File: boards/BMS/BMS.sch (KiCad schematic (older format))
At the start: 51 parts

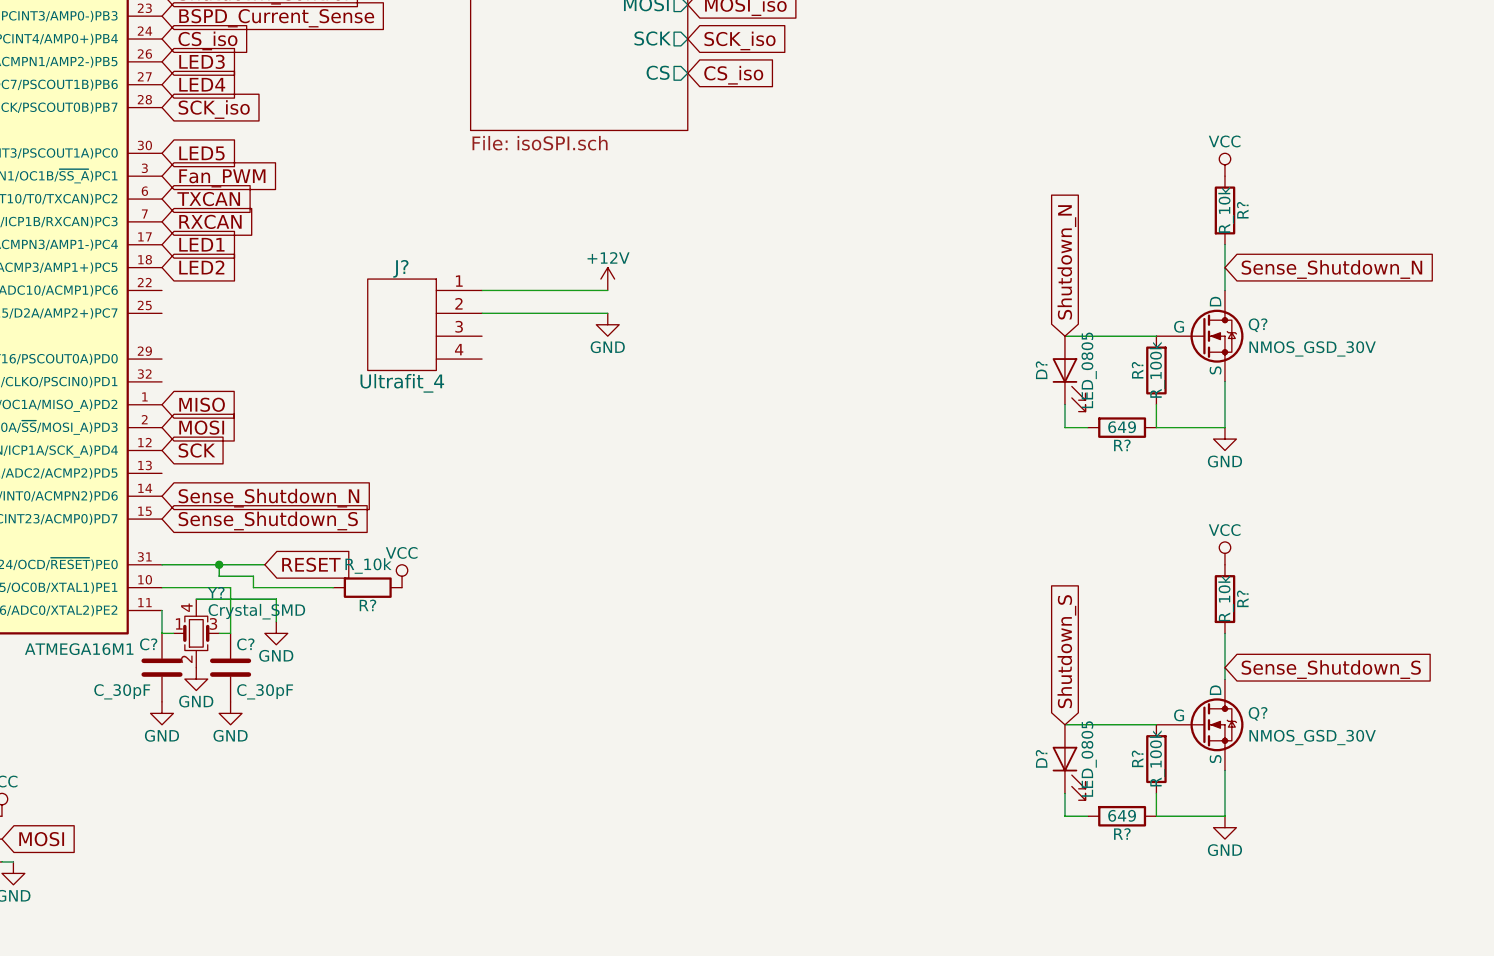
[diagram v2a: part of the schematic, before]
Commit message: Completed recreation of BMS master
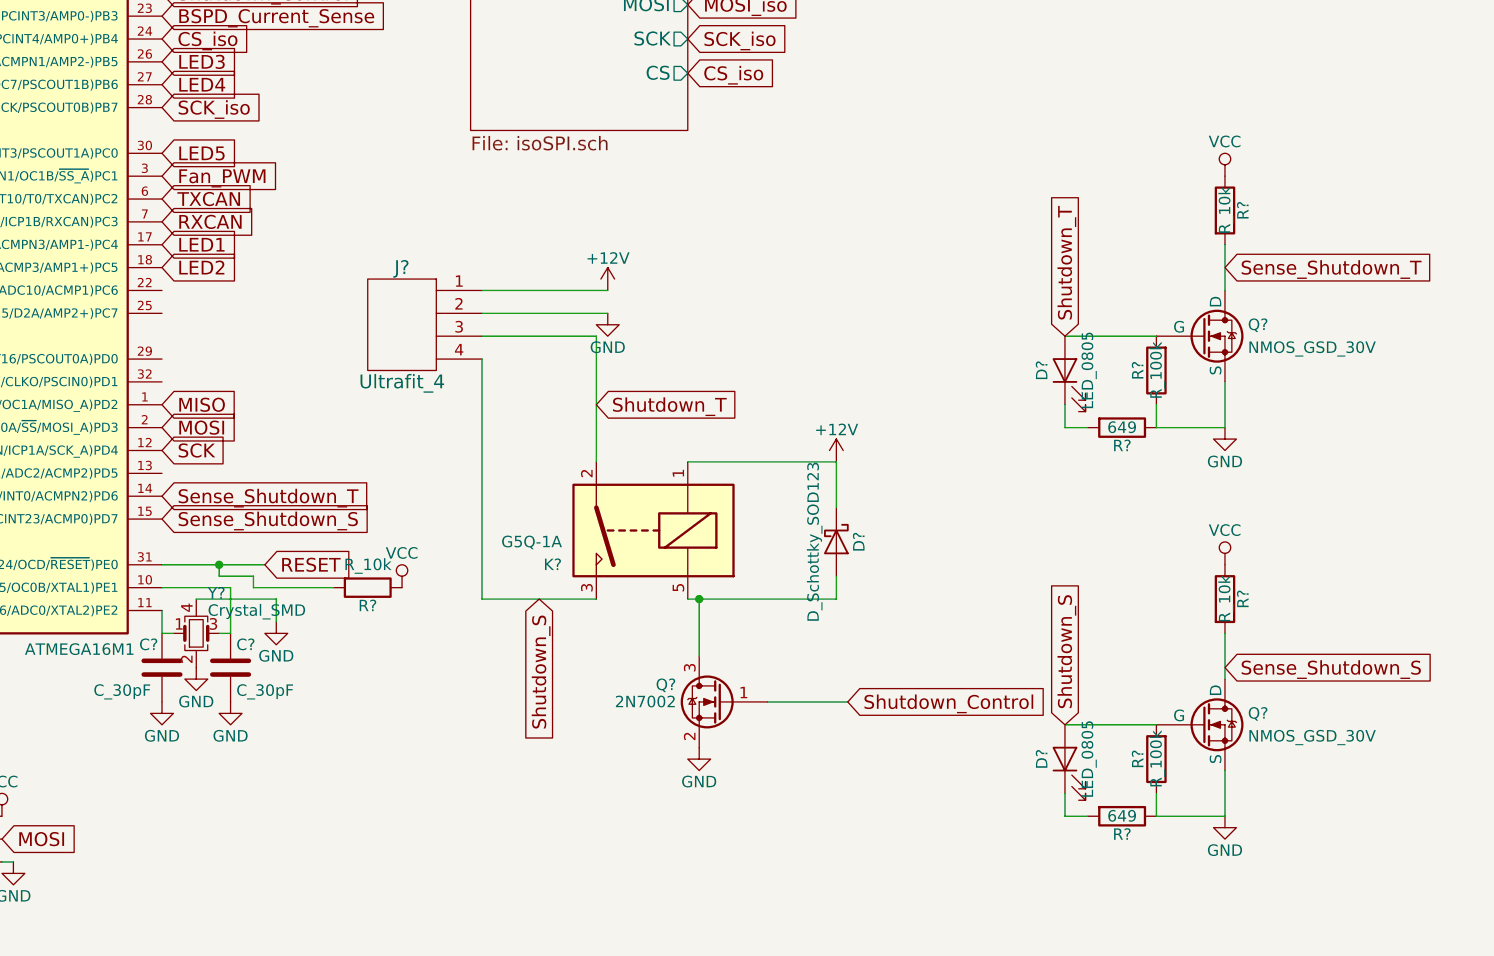
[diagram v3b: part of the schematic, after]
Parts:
- added D?: D_Schottky_SOD123, Diodes_SMD:D_SOD-123, symbol D_Schottky_SOD123
- added K?: G5Q-1A, Relays_THT:Relay_SPST-NO_OMRON-G5Q, symbol G5Q-1A
- added Q?: 2N7002, TO_SOT_Packages_SMD:SOT-23, symbol 2N7002
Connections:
- net Shutdown_N is gone; now on net Shutdown_T: D?.2 (A), Q?.1 (G), R?.2
- net +12V: now also D?.1 (K), K?.1
- net GND: now also Q?.2 (S)
- net Shutdown_Control: now also Q?.1 (G)
- net Shutdown_S: now also J?.4, K?.3
- net Shutdown_T: now reaches J?.3
- net Shutdown_T: now also K?.2
- net Sense_Shutdown_N renamed Sense_Shutdown_T
- new net: D?.2 (A), K?.5, Q?.3 (D)
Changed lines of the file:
@@
 Shutdown_S
 Text GLabel 8000 4250 1    60   Input ~ 0
-Shutdown_N
+Shutdown_T
 Text GLabel 8700 3950 2    60   Input ~ 0
-Sense_Shutdown_N
+Sense_Shutdown_T
 Text GLabel 8700 5700 2    60   Input ~ 0
 Sense_Shutdown_S
@@
 Sense_Shutdown_S
 Text GLabel 4050 4950 2    60   Input ~ 0
-Sense_Shutdown_N
+Sense_Shutdown_T
 Wire Wire Line
 	4300 5250 4300 5300
@@
 Wire Wire Line
 	5300 1400 5700 1400
+$Comp
+L G5Q-1A K?
+U 1 1 59E94541
+P 6350 4900
+F 0 "K?" H 6900 5250 50  0000 L CNN
+F 1 "G5Q-1A" H 6900 5150 50  0000 L CNN
+F 2 "Relays_THT:Relay_SPST-NO_OMRON-G5Q" H 6900 5050 50  0001 L CNN
+F 3 "" H 7450 4600 50  0001 C CNN
+	1    6350 4900
+	-1   0    0    1
+$EndComp
+Wire Wire Line
+	5450 4250 5950 4250
+Wire Wire Line
+	5950 4250 5950 4800
+Wire Wire Line
+	5450 4350 5450 5400
+Wire Wire Line
+	5450 5400 5950 5400
+Text GLabel 5950 4550 2    60   Input ~ 0
+Shutdown_T
+Text GLabel 5700 5400 3    60   Input ~ 0
+Shutdown_S
+$Comp
+L D_Schottky_SOD123 D?
+U 1 1 59E96256
+P 7000 5150
+F 0 "D?" H 7000 5250 50  0000 C CNN
+F 1 "D_Schottky_SOD123" H 7000 5050 50  0000 C CNN
+F 2 "Diodes_SMD:D_SOD-123" H 6900 5150 50  0001 C CNN
+F 3 "https://assets.nexperia.com/documents/data-sheet/PMEG10010ELR.pdf" H 7000 5250 50  0001 C CNN
+F 4 "1727-2394-1-ND" H 7100 5350 60  0001 C CNN "MPN"
+F 5 "Digi-Key" H 7200 5450 60  0001 C CNN "MFN"
+F 6 "https://www.digikey.com/product-detail/en/nexperia-usa-inc/PMEG10010ELRX/1727-2394-1-ND/5436140" H 7300 5550 60  0001 C CNN "PurchasingLink"
+	1    7000 5150
+	0    1    1    0
+$EndComp
+Wire Wire Line
+	6350 4800 7000 4800
+Wire Wire Line
+	7000 4800 7000 5000
+Wire Wire Line
+	6350 5400 7000 5400
+Wire Wire Line
+	7000 5400 7000 5300
+$Comp
+L 2N7002 Q?
+U 1 1 59E96A45
+P 6500 5850
+F 0 "Q?" H 6700 5925 50  0000 L CNN
+F 1 "2N7002" H 6700 5850 50  0000 L CNN
+F 2 "TO_SOT_Packages_SMD:SOT-23" H 6700 5775 50  0001 L CIN
+F 3 "" H 6500 5850 50  0001 L CNN
+	1    6500 5850
+	-1   0    0    -1
+$EndComp
+Wire Wire Line
+	6400 5650 6400 5400
+Connection ~ 6400 5400
+Wire Wire Line
+	6700 5850 7050 5850
+$Comp
+L GND #PWR?
+U 1 1 59E96FA5
+P 6400 6050
+F 0 "#PWR?" H 6400 5800 50  0001 C CNN
+F 1 "GND" H 6400 5900 50  0000 C CNN
+F 2 "" H 6400 6050 50  0001 C CNN
+F 3 "" H 6400 6050 50  0001 C CNN
+	1    6400 6050
+	1    0    0    -1
+$EndComp
+$Comp
+L +12V #PWR?
+U 1 1 59E972B6
+P 7000 4800
+F 0 "#PWR?" H 7000 4650 50  0001 C CNN
+F 1 "+12V" H 7000 4940 50  0000 C CNN
+F 2 "" H 7000 4800 50  0001 C CNN
+F 3 "" H 7000 4800 50  0001 C CNN
+	1    7000 4800
+	1    0    0    -1
+$EndComp
+Text GLabel 7050 5850 2    60   Input ~ 0
+Shutdown_Control
 $EndSCHEMATC

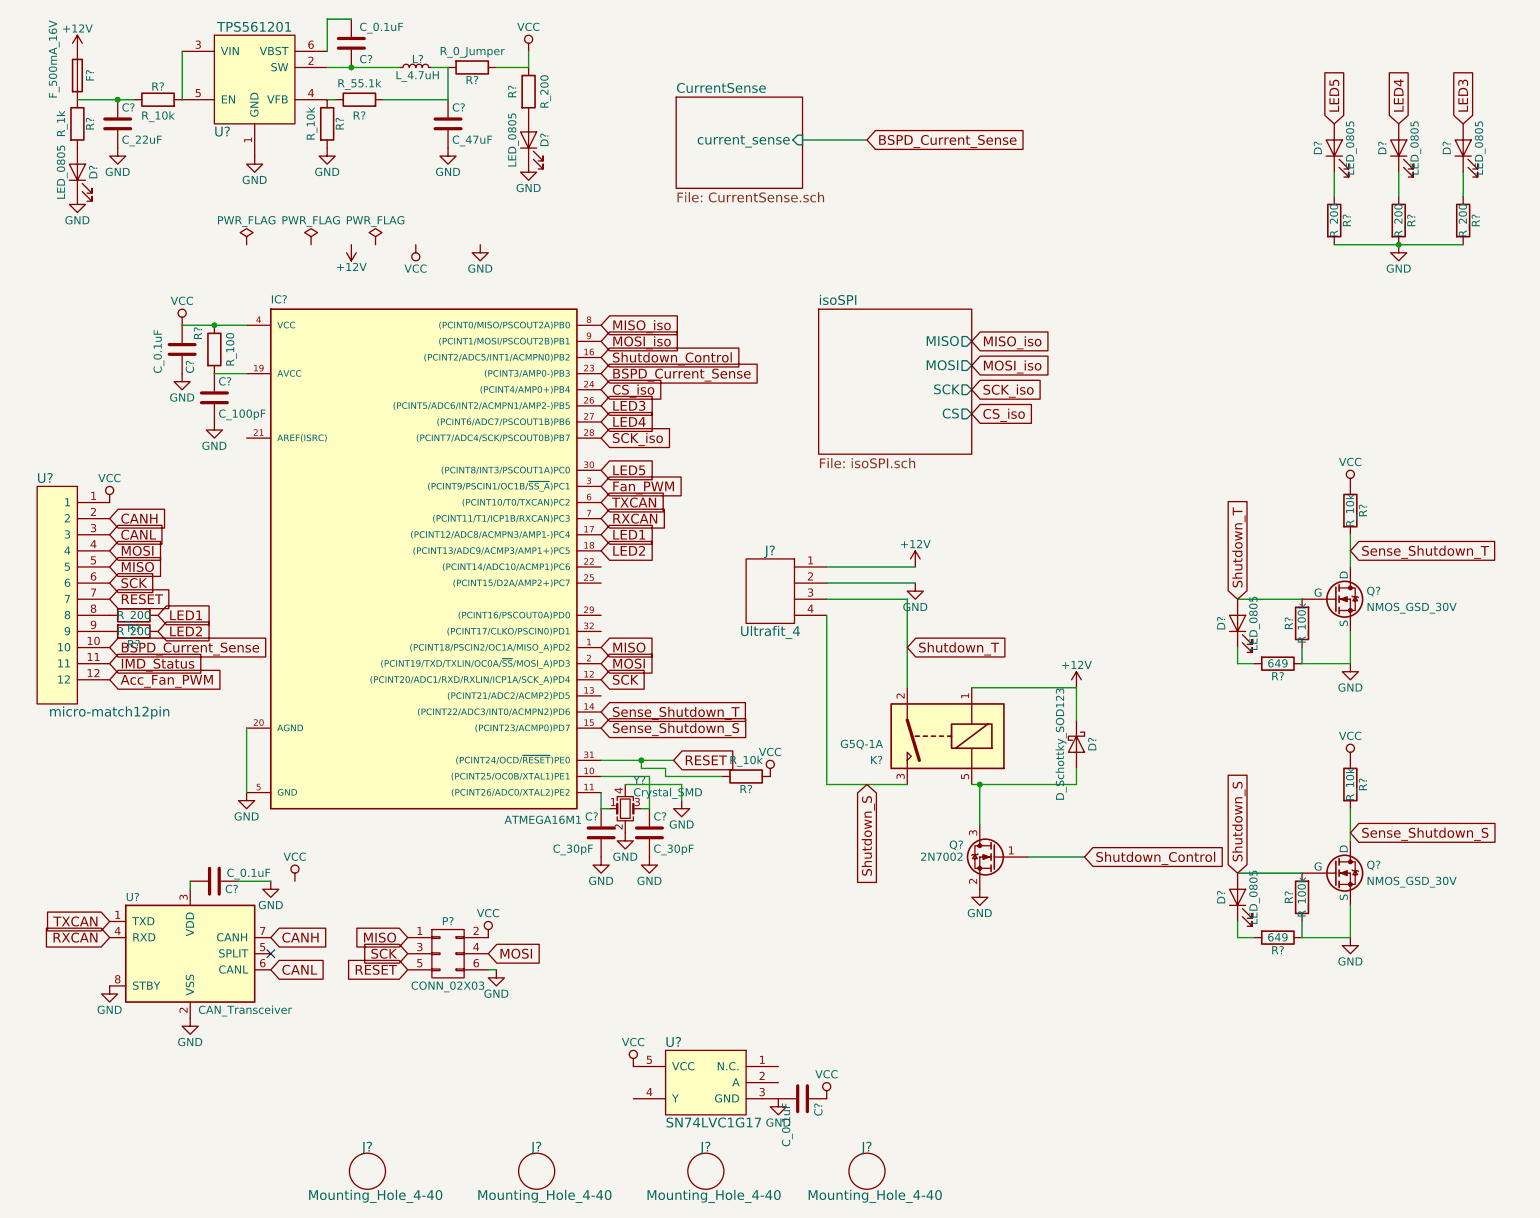
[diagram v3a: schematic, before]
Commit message: edited discharge circuit schematic
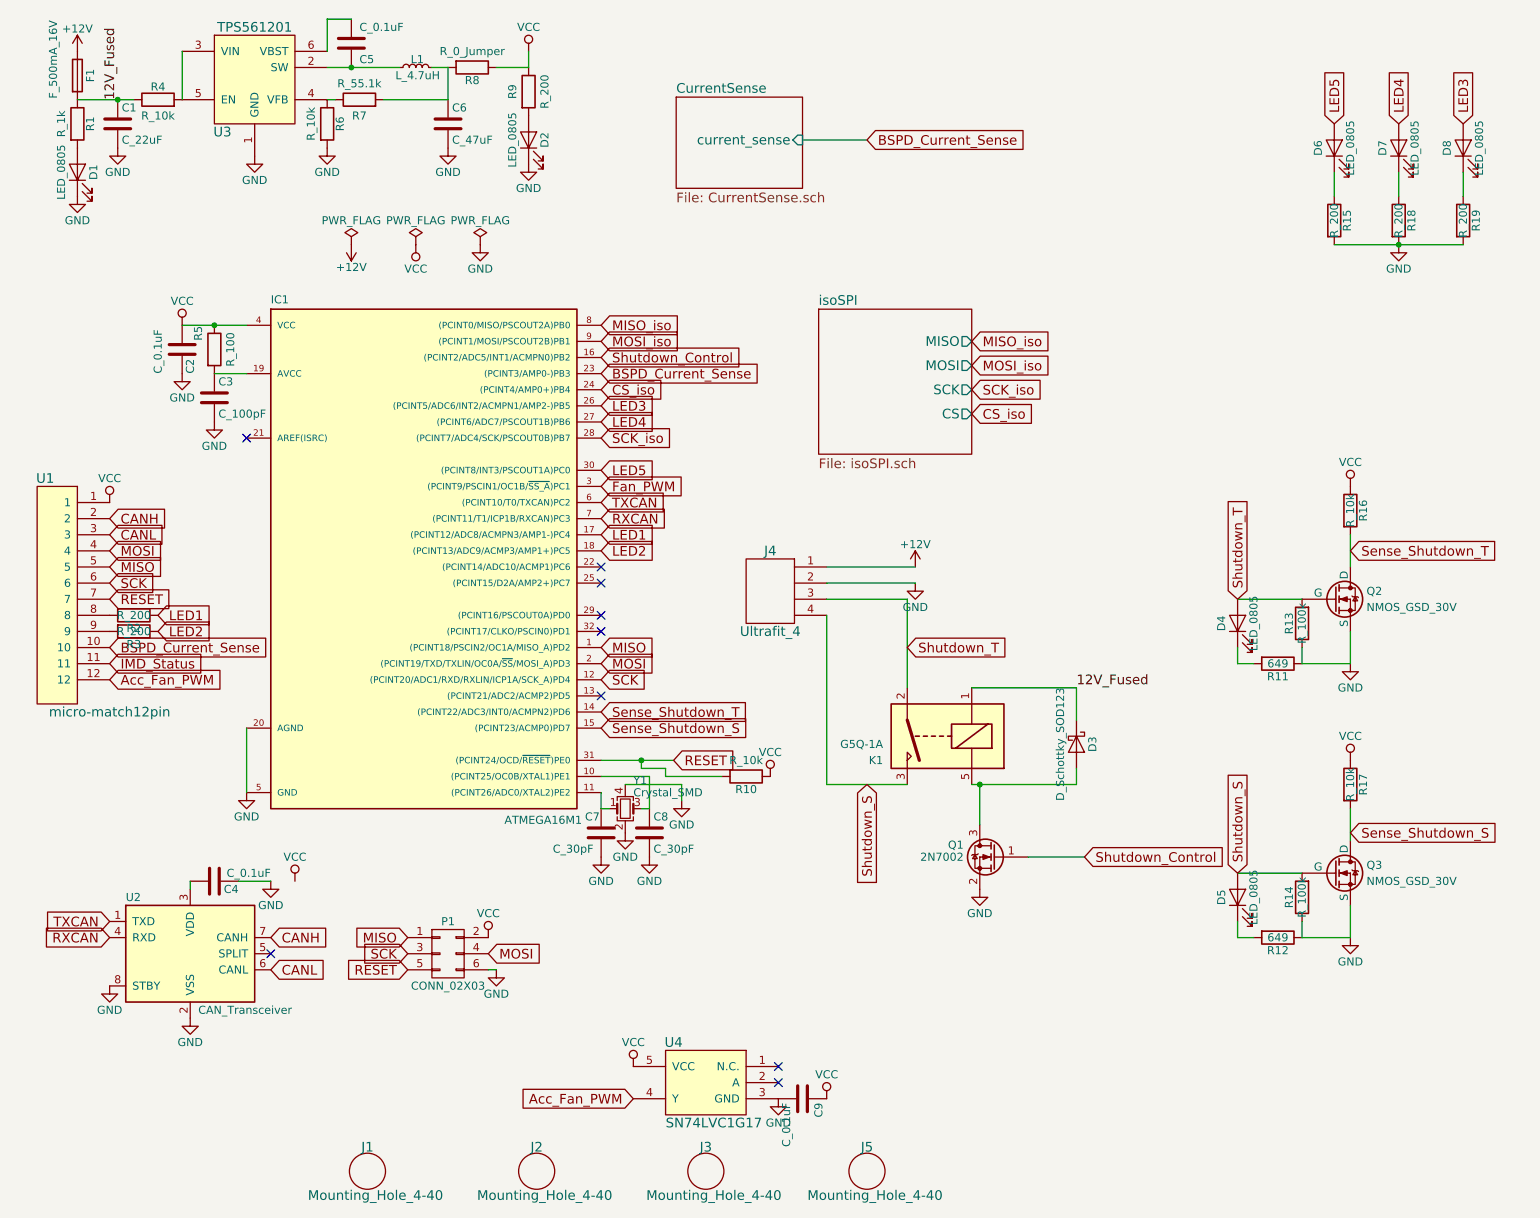
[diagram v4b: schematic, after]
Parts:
- gave numbers to parts that had none: 54
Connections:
- net +12V: no longer D3.1 (K), K1.1
- net Acc_Fan_PWM: now also U4.4 (Y)
- net 12V_Fused: now reaches C1.1, F1.2, R1.1, R4.1
- net 12V_Fused: now also D3.1 (K), K1.1
- no-connect marks 1 -> 9

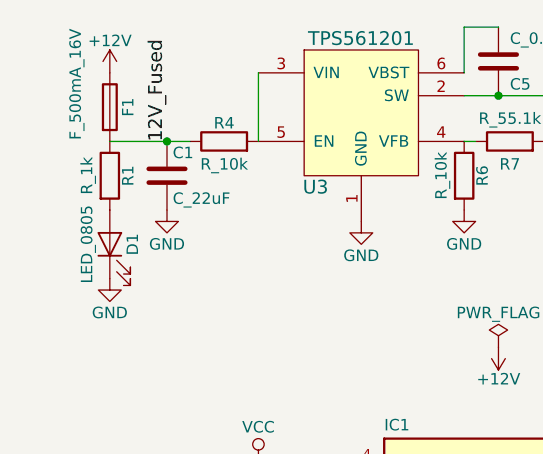
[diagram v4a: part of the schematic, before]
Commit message: Added isoSPI parts and fuses
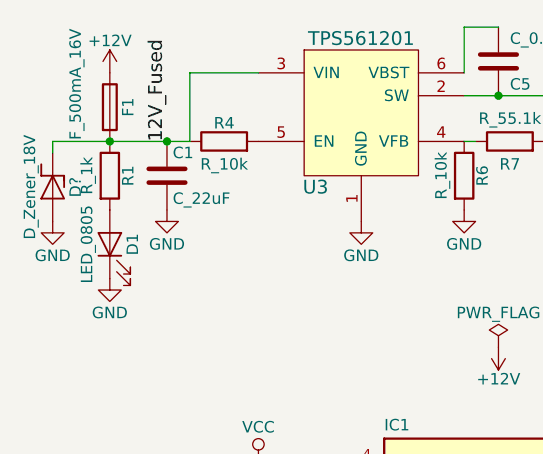
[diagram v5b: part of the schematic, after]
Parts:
- added D?: D_Zener_18V, footprints:DO-214AA, symbol D_Zener_18V
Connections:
- net 12V_Fused: now also U3.3 (VIN), D?.1 (K)
- net GND: now also D?.2 (A)
- net at R4.2, U3.5 (EN): no longer U3.3 (VIN)
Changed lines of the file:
@@
 Shutdown_Control
-Wire Wire Line
-	1450 850  1450 1150
 Wire Wire Line
 	2350 950  2800 950
@@
 Connection ~ 1650 2550
 Wire Wire Line
-	800  1150 1150 1150
+	550  1150 1150 1150
 Connection ~ 1050 1150
 Wire Wire Line
@@
 Text GLabel 4250 7350 0    60   Input ~ 0
 Acc_Fan_PWM
+Wire Wire Line
+	1450 850  1150 850
+Wire Wire Line
+	1150 850  1150 1150
+$Comp
+L D_Zener_18V D?
+U 1 1 59F839F9
+P 550 1350
+F 0 "D?" H 550 1450 50  0000 C CNN
+F 1 "D_Zener_18V" H 550 1250 50  0000 C CNN
+F 2 "footprints:DO-214AA" H 450 1350 50  0001 C CNN
+F 3 "http://www.mccsemi.com/up_pdf/SMBJ5338B-SMBJ5388B(SMB).pdf" H 550 1450 50  0001 C CNN
+F 4 "SMBJ5355B-TPMSCT-ND" H 650 1550 60  0001 C CNN "MPN"
+F 5 "Digi-Key" H 750 1650 60  0001 C CNN "MFN"
+F 6 "DO-214AA (SMB)" H 850 1750 60  0001 C CNN "Package"
+F 7 "https://www.digikey.com/products/en?keywords=SMBJ5355B-TPMSCT-ND" H 950 1850 60  0001 C CNN "PurchasingLink"
+	1    550  1350
+	0    1    1    0
+$EndComp
+Wire Wire Line
+	550  1200 550  1150
+Connection ~ 800  1150
+$Comp
+L GND #PWR?
+U 1 1 59F83B8F
+P 550 1500
+F 0 "#PWR?" H 550 1250 50  0001 C CNN
+F 1 "GND" H 550 1350 50  0000 C CNN
+F 2 "" H 550 1500 50  0001 C CNN
+F 3 "" H 550 1500 50  0001 C CNN
+	1    550  1500
+	1    0    0    -1
+$EndComp
 $EndSCHEMATC
